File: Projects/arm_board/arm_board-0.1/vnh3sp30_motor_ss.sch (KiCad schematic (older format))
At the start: 3 parts

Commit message: Arm Board: bug fixes, and added footprints
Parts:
- removed P?: CONN_6, ~, symbol CONN_6
- added P1: CONN_5, ArmFootprints:5-pin_640467-1, symbol CONN_5
- added R23: 4.7k, Resistors_SMD:R_0805, symbol R
- added R39, R40: 1k, Resistors_SMD:R_0805, symbol R
- U14: renamed from U?; footprint (none) -> ArmFootprints:SN74LVC2G08DCTR
- VNH3: renamed from VNH1; footprint (none) -> ArmFootprints:VNH3SP30TR-E
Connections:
- net labels added: NOISE_5V, n_CNT_RESET
- net labels removed: CNT_RESET, EN
- wire segments 66 -> 71
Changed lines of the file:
@@
 LIBS:ArmComponentLibrary
 LIBS:arm_board-cache
-EELAYER 27 0
+EELAYER 25 0
 EELAYER END
 $Descr A4 11693 8268
@@
 $EndDescr
 $Comp
-L VNH3SP30 VNH1
+L VNH3SP30 VNH3
 U 1 1 564A6239
 P 8550 3800
-AR Path="/564B31DF/564A6239" Ref="VNH1"  Part="1"
-AR Path="/56666F75/564A6239" Ref="VNH1"  Part="1"
-AR Path="/56669634/564A6239" Ref="VNH1"  Part="1"
-AR Path="/56669644/564A6239" Ref="VNH1"  Part="1"
-AR Path="/5666D2E0/564A6239" Ref="VNH1"  Part="1"
-AR Path="/5666D2F0/564A6239" Ref="VNH1"  Part="1"
-AR Path="/56F5245F/564A6239" Ref="VNH1"  Part="1"
-AR Path="/56F544AF/564A6239" Ref="VNH1"  Part="1"
-F 0 "VNH1" H 9250 2850 60  0000 C CNN
+AR Path="/56F5245F/564A6239" Ref="VNH3"  Part="1"
+AR Path="/56F53B7D/564A6239" Ref="VNH4"  Part="1"
+AR Path="/56F544AF/564A6239" Ref="VNH5"  Part="1"
+AR Path="/56F55E0D/564A6239" Ref="VNH6"  Part="1"
+AR Path="/56F56B2F/564A6239" Ref="VNH7"  Part="1"
+F 0 "VNH4" H 9250 2850 60  0000 C CNN
 F 1 "VNH3SP30" H 8550 3800 60  0000 C CNN
-F 2 "" H 6950 3600 60  0000 C CNN
+F 2 "ArmFootprints:VNH3SP30TR-E" H 6950 3600 60  0001 C CNN
 F 3 "" H 6950 3600 60  0000 C CNN
 	1    8550 3800
@@
 	8550 5250 8550 4900
 Connection ~ 8550 4900
-Text HLabel 7250 3750 0    60   Input ~ 0
+Text HLabel 6800 3750 0    60   Input ~ 0
 DIR
-Text HLabel 7250 3850 0    60   Input ~ 0
+Text HLabel 6650 3850 0    60   Input ~ 0
 n_DIR
 Text HLabel 7250 4000 0    60   Input ~ 0
@@
 Wire Wire Line
 	7250 4000 7700 4000
-Wire Wire Line
-	7250 3850 7700 3850
-Wire Wire Line
-	7250 3750 7700 3750
-Wire Wire Line
-	7250 3500 7700 3500
 $Sheet
 S 5250 4600 1100 1000
@@
 F5 "CNT_UP" I L 5250 4700 60
 F6 "CNT_DWN" I L 5250 4800 60
-F7 "RESET" I L 5250 5000 60
-F8 "S0" I L 5250 5200 60
-F9 "S1" I L 5250 5300 60
-F10 "S2" I L 5250 5400 60
-F11 "S3" I L 5250 5500 60
+F7 "S0" I L 5250 5200 60
+F8 "S1" I L 5250 5300 60
+F9 "S2" I L 5250 5400 60
+F10 "S3" I L 5250 5500 60
+F11 "n_RESET" I L 5250 5000 60
 $EndSheet
 Wire Wire Line
@@
 	7550 3600 7550 3500
 Connection ~ 7550 3500
-Text HLabel 7250 3500 0    60   Input ~ 0
-EN
-Text Label 7350 3750 0    60   ~ 0
+Text Label 6750 3600 2    60   ~ 0
 DIR
-Text Label 7350 3850 0    60   ~ 0
+Text Label 6650 4050 2    60   ~ 0
 n_DIR
 $Comp
-L 74LVC2G08 U?
+L 74LVC2G08 U14
 U 1 1 565DD202
 P 4650 4850
-AR Path="/564B31DF/565DD202" Ref="U?"  Part="1"
-AR Path="/56666F75/565DD202" Ref="U?"  Part="1"
-AR Path="/56669634/565DD202" Ref="U?"  Part="1"
-AR Path="/56669644/565DD202" Ref="U?"  Part="1"
-AR Path="/5666D2E0/565DD202" Ref="U?"  Part="1"
-AR Path="/5666D2F0/565DD202" Ref="U?"  Part="1"
-AR Path="/56F5245F/565DD202" Ref="U?"  Part="1"
-AR Path="/56F544AF/565DD202" Ref="U?"  Part="1"
-F 0 "U?" H 4750 4450 60  0000 C CNN
+AR Path="/56F5245F/565DD202" Ref="U14"  Part="1"
+AR Path="/56F53B7D/565DD202" Ref="U21"  Part="1"
+AR Path="/56F544AF/565DD202" Ref="U28"  Part="1"
+AR Path="/56F55E0D/565DD202" Ref="U35"  Part="1"
+AR Path="/56F56B2F/565DD202" Ref="U42"  Part="1"
+F 0 "U21" H 4750 4450 60  0000 C CNN
 F 1 "74LVC2G08" V 4500 4900 60  0000 C CNN
-F 2 "" H 4650 4850 60  0000 C CNN
+F 2 "ArmFootprints:SN74LVC2G08DCTR" H 4650 4850 60  0001 C CNN
 F 3 "" H 4650 4850 60  0000 C CNN
 	1    4650 4850
@@
 CNT_UDRFLW
 Text HLabel 4850 5650 0    60   Output ~ 0
-CNT_RESET
+n_CNT_RESET
 Text HLabel 4850 5750 0    60   Output ~ 0
 CNT_S0
@@
 	9400 3950 9400 4150
 Connection ~ 9400 4050
-$Comp
-L CONN_6 P?
-U 1 1 56F466A7
-P 10750 5750
-AR Path="/564B31DF/56F466A7" Ref="P?"  Part="1"
-AR Path="/56F5245F/56F466A7" Ref="P?"  Part="1"
-AR Path="/56F544AF/56F466A7" Ref="P?"  Part="1"
-F 0 "P?" V 10700 5750 60  0000 C CNN
-F 1 "CONN_6" V 10800 5750 60  0000 C CNN
-F 2 "~" H 10750 5750 60  0000 C CNN
-F 3 "~" H 10750 5750 60  0000 C CNN
-	1    10750 5750
-	1    0    0    -1
-$EndComp
 Wire Wire Line
 	9800 3550 9800 5500
@@
 Wire Wire Line
 	9700 4050 9400 4050
+$Comp
+L R R39
+U 1 1 56C5F3D4
+P 7450 3750
+AR Path="/56F53B7D/56C5F3D4" Ref="R39"  Part="1"
+AR Path="/56F5245F/56C5F3D4" Ref="R24"  Part="1"
+AR Path="/56F544AF/56C5F3D4" Ref="R27"  Part="1"
+AR Path="/56F55E0D/56C5F3D4" Ref="R30"  Part="1"
+AR Path="/56F56B2F/56C5F3D4" Ref="R33"  Part="1"
+F 0 "R39" V 7530 3750 40  0000 C CNN
+F 1 "1k" V 7457 3751 40  0000 C CNN
+F 2 "Resistors_SMD:R_0805" V 7380 3750 30  0001 C CNN
+F 3 "" H 7450 3750 30  0000 C CNN
+	1    7450 3750
+	0    1    1    0
+$EndComp
+Wire Wire Line
+	6800 3750 7200 3750
+Wire Wire Line
+	6750 3600 6900 3600
+Wire Wire Line
+	6900 3600 6900 3750
+Connection ~ 6900 3750
+$Comp
+L R R40
+U 1 1 56C5F9C5
+P 7450 3850
+AR Path="/56F53B7D/56C5F9C5" Ref="R40"  Part="1"
+AR Path="/56F5245F/56C5F9C5" Ref="R25"  Part="1"
+AR Path="/56F544AF/56C5F9C5" Ref="R28"  Part="1"
+AR Path="/56F55E0D/56C5F9C5" Ref="R31"  Part="1"
+AR Path="/56F56B2F/56C5F9C5" Ref="R34"  Part="1"
+F 0 "R40" V 7530 3850 40  0000 C CNN
+F 1 "1k" V 7457 3851 40  0000 C CNN
+F 2 "Resistors_SMD:R_0805" V 7380 3850 30  0001 C CNN
+F 3 "" H 7450 3850 30  0000 C CNN
+	1    7450 3850
+	0    1    1    0
+$EndComp
+Wire Wire Line
+	7200 3850 6650 3850
+Wire Wire Line
+	6650 4050 6800 4050
+Wire Wire Line
+	6800 4050 6800 3850
+Connection ~ 6800 3850
+Wire Wire Line
+	7550 3500 7700 3500
+$Comp
+L R R23
+U 1 1 56C6696F
+P 7300 3500
+AR Path="/56F5245F/56C6696F" Ref="R23"  Part="1"
+AR Path="/56F544AF/56C6696F" Ref="R26"  Part="1"
+AR Path="/56F55E0D/56C6696F" Ref="R29"  Part="1"
+AR Path="/56F56B2F/56C6696F" Ref="R32"  Part="1"
+AR Path="/56F53B7D/56C6696F" Ref="R38"  Part="1"
+F 0 "R38" V 7380 3500 40  0000 C CNN
+F 1 "4.7k" V 7307 3501 40  0000 C CNN
+F 2 "Resistors_SMD:R_0805" V 7230 3500 30  0001 C CNN
+F 3 "" H 7300 3500 30  0000 C CNN
+	1    7300 3500
+	0    1    1    0
+$EndComp
+Text GLabel 7050 3250 1    60   Input ~ 0
+NOISE_5V
+Wire Wire Line
+	7050 3250 7050 3500
+$Comp
+L CONN_5 P1
+U 1 1 56CA7E11
+P 10800 5700
+AR Path="/56F5245F/56CA7E11" Ref="P1"  Part="1"
+AR Path="/56F53B7D/56CA7E11" Ref="P10"  Part="1"
+AR Path="/56F544AF/56CA7E11" Ref="P2"  Part="1"
+AR Path="/56F55E0D/56CA7E11" Ref="P7"  Part="1"
+AR Path="/56F56B2F/56CA7E11" Ref="P8"  Part="1"
+F 0 "P10" V 10750 5700 50  0000 C CNN
+F 1 "CONN_5" V 10850 5700 50  0000 C CNN
+F 2 "ArmFootprints:5-pin_640467-1" H 10800 5700 60  0001 C CNN
+F 3 "" H 10800 5700 60  0000 C CNN
+	1    10800 5700
+	1    0    0    -1
+$EndComp
 $EndSCHEMATC

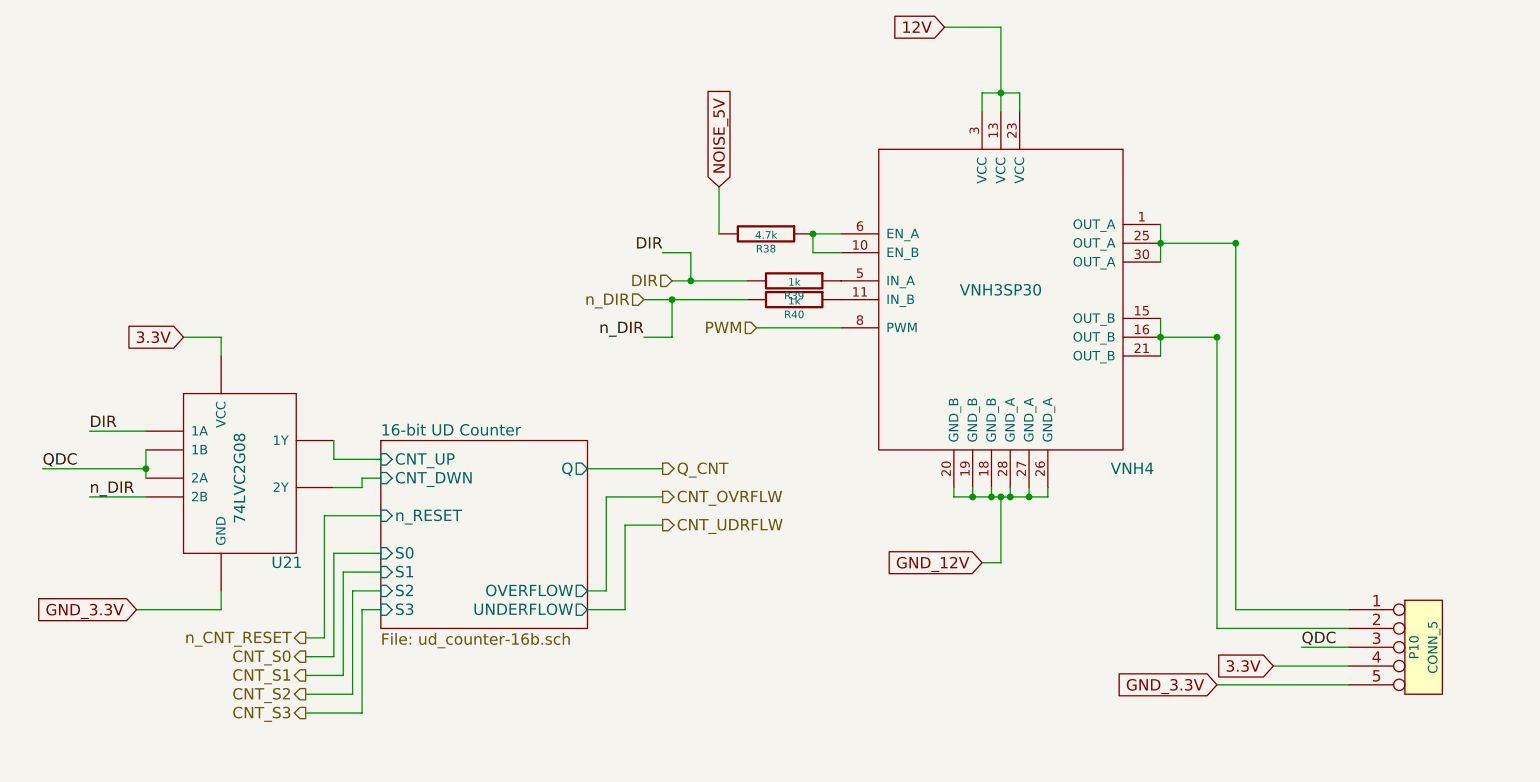
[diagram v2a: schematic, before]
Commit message: Arm Board: bug fixes, cleanup, and start PCB layout
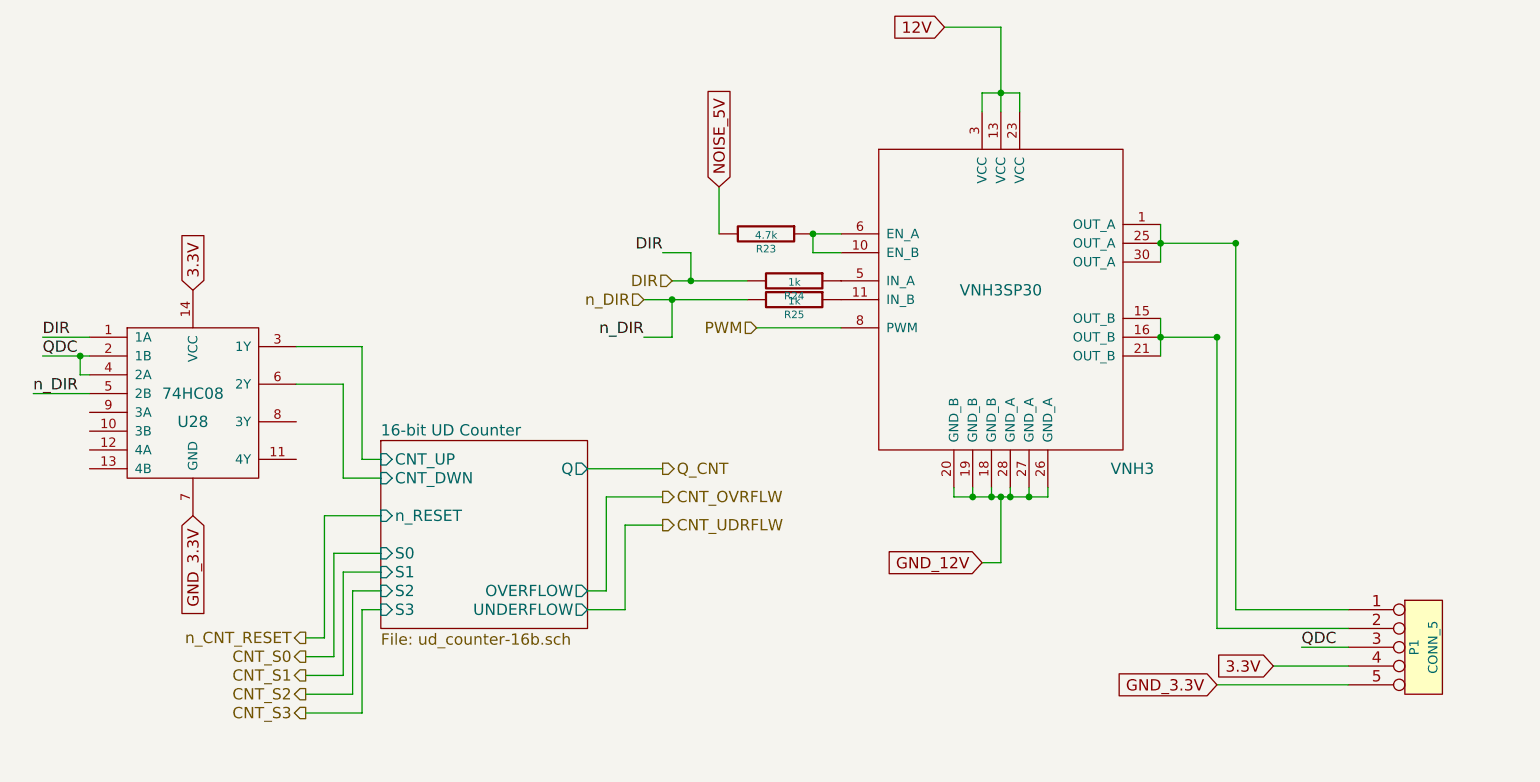
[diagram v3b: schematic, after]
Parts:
- removed U14: 74LVC2G08, ArmFootprints:SN74LVC2G08DCTR, symbol 74LVC2G08
- added U28: 74HC08, SMD_Packages:SOIC-14_N, symbol 74HC08
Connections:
- net 16-bit UD Counter/CNT_DWN: now also U28.6 (2Y)
- net 16-bit UD Counter/CNT_UP: now also U28.3 (1Y)
- net 3.3V: now also U28.14 (VCC)
- net DIR: now also U28.1 (1A)
- net GND_3.3V: now also U28.7 (GND)
- net QDC: now also U28.2 (1B), U28.4 (2A)
- net n_DIR: now also U28.5 (2B)
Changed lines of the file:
@@
 AR Path="/56F55E0D/564A6239" Ref="VNH6"  Part="1"
 AR Path="/56F56B2F/564A6239" Ref="VNH7"  Part="1"
-F 0 "VNH4" H 9250 2850 60  0000 C CNN
+F 0 "VNH3" H 9250 2850 60  0000 C CNN
 F 1 "VNH3SP30" H 8550 3800 60  0000 C CNN
 F 2 "ArmFootprints:VNH3SP30TR-E" H 6950 3600 60  0001 C CNN
@@
 Text Label 6650 4050 2    60   ~ 0
 n_DIR
-$Comp
-L 74LVC2G08 U14
-U 1 1 565DD202
-P 4650 4850
-AR Path="/56F5245F/565DD202" Ref="U14"  Part="1"
-AR Path="/56F53B7D/565DD202" Ref="U21"  Part="1"
-AR Path="/56F544AF/565DD202" Ref="U28"  Part="1"
-AR Path="/56F55E0D/565DD202" Ref="U35"  Part="1"
-AR Path="/56F56B2F/565DD202" Ref="U42"  Part="1"
-F 0 "U21" H 4750 4450 60  0000 C CNN
-F 1 "74LVC2G08" V 4500 4900 60  0000 C CNN
-F 2 "ArmFootprints:SN74LVC2G08DCTR" H 4650 4850 60  0001 C CNN
-F 3 "" H 4650 4850 60  0000 C CNN
-	1    4650 4850
-	1    0    0    -1
-$EndComp
-Text Label 3450 4750 0    60   ~ 0
-QDC
-Wire Wire Line
-	3450 4750 4000 4750
-Wire Wire Line
-	4000 4650 4000 4800
-Connection ~ 4000 4750
-Text Label 3700 4550 0    60   ~ 0
-DIR
-Text Label 3700 4900 0    60   ~ 0
-n_DIR
-Wire Wire Line
-	3700 4900 4000 4900
-Wire Wire Line
-	4000 4550 3700 4550
-Text GLabel 4200 4050 0    60   Input ~ 0
-3.3V
-Wire Wire Line
-	4200 4050 4400 4050
-Wire Wire Line
-	4400 4050 4400 4150
-Text GLabel 3950 5500 0    60   Input ~ 0
-GND_3.3V
-Wire Wire Line
-	3950 5500 4400 5500
-Wire Wire Line
-	4400 5500 4400 5400
-Wire Wire Line
-	5000 4600 5000 4700
-Wire Wire Line
-	5000 4700 5250 4700
-Wire Wire Line
-	5000 4850 5150 4850
-Wire Wire Line
-	5150 4850 5150 4800
-Wire Wire Line
-	5150 4800 5250 4800
 Text HLabel 6750 4750 2    60   Output ~ 0
 Q_CNT
@@
 AR Path="/56F55E0D/56C5F3D4" Ref="R30"  Part="1"
 AR Path="/56F56B2F/56C5F3D4" Ref="R33"  Part="1"
-F 0 "R39" V 7530 3750 40  0000 C CNN
+F 0 "R24" V 7530 3750 40  0000 C CNN
 F 1 "1k" V 7457 3751 40  0000 C CNN
 F 2 "Resistors_SMD:R_0805" V 7380 3750 30  0001 C CNN
@@
 AR Path="/56F55E0D/56C5F9C5" Ref="R31"  Part="1"
 AR Path="/56F56B2F/56C5F9C5" Ref="R34"  Part="1"
-F 0 "R40" V 7530 3850 40  0000 C CNN
+F 0 "R25" V 7530 3850 40  0000 C CNN
 F 1 "1k" V 7457 3851 40  0000 C CNN
 F 2 "Resistors_SMD:R_0805" V 7380 3850 30  0001 C CNN
@@
 AR Path="/56F56B2F/56C6696F" Ref="R32"  Part="1"
 AR Path="/56F53B7D/56C6696F" Ref="R38"  Part="1"
-F 0 "R38" V 7380 3500 40  0000 C CNN
+F 0 "R23" V 7380 3500 40  0000 C CNN
 F 1 "4.7k" V 7307 3501 40  0000 C CNN
 F 2 "Resistors_SMD:R_0805" V 7230 3500 30  0001 C CNN
@@
 AR Path="/56F55E0D/56CA7E11" Ref="P7"  Part="1"
 AR Path="/56F56B2F/56CA7E11" Ref="P8"  Part="1"
-F 0 "P10" V 10750 5700 50  0000 C CNN
+F 0 "P1" V 10750 5700 50  0000 C CNN
 F 1 "CONN_5" V 10850 5700 50  0000 C CNN
 F 2 "ArmFootprints:5-pin_640467-1" H 10800 5700 60  0001 C CNN
@@
 	1    0    0    -1
 $EndComp
+Text GLabel 4250 3800 1    60   Input ~ 0
+3.3V
+Text GLabel 4250 5000 3    60   Input ~ 0
+GND_3.3V
+$Comp
+L 74HC08 U28
+U 1 1 56CE991E
+P 4250 4350
+AR Path="/56F5245F/56CE991E" Ref="U28"  Part="1"
+AR Path="/56F53B7D/56CE991E" Ref="U58"  Part="1"
+AR Path="/56F544AF/56CE991E" Ref="U35"  Part="1"
+AR Path="/56F55E0D/56CE991E" Ref="U42"  Part="1"
+AR Path="/56F56B2F/56CE991E" Ref="U44"  Part="1"
+F 0 "U28" H 4250 4200 60  0000 C CNN
+F 1 "74HC08" H 4250 4350 60  0000 C CNN
+F 2 "SMD_Packages:SOIC-14_N" H 4250 4350 60  0001 C CNN
+F 3 "" H 4250 4350 60  0000 C CNN
+	1    4250 4350
+	1    0    0    -1
+$EndComp
+Text Label 3450 4150 0    60   ~ 0
+QDC
+Text Label 3450 4050 0    60   ~ 0
+DIR
+Text Label 3400 4350 0    60   ~ 0
+n_DIR
+Wire Wire Line
+	3450 4050 3700 4050
+Wire Wire Line
+	3450 4150 3700 4150
+Wire Wire Line
+	3650 4150 3650 4250
+Wire Wire Line
+	3650 4250 3700 4250
+Connection ~ 3650 4150
+Wire Wire Line
+	3400 4350 3700 4350
+Wire Wire Line
+	4800 4100 5150 4100
+Wire Wire Line
+	5150 4100 5150 4700
+Wire Wire Line
+	5150 4700 5250 4700
+Wire Wire Line
+	4800 4300 5050 4300
+Wire Wire Line
+	5050 4300 5050 4800
+Wire Wire Line
+	5050 4800 5250 4800
 $EndSCHEMATC

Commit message: Arm Board: finalizing footprints.
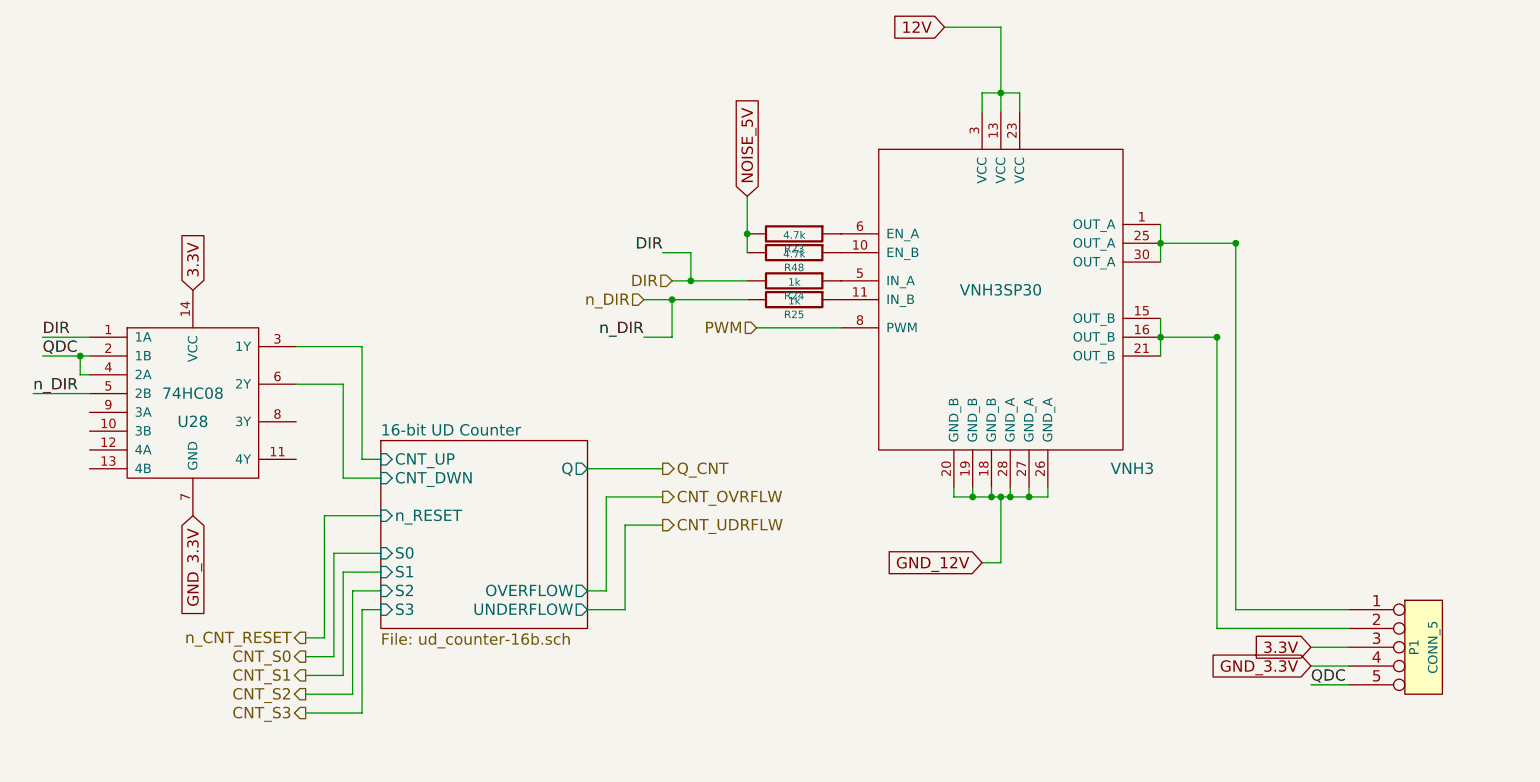
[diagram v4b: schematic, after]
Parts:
- added R53: 4.7k, Resistors_SMD:R_0805, symbol R
- U28: footprint SMD_Packages:SOIC-14_N -> ArmFootprints:SOIC-14
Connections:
- net 3.3V: now also P1.3; no longer P1.4
- net GND_3.3V: now also P1.4; no longer P1.5
- net NOISE_5V: now also R53.2
- net QDC: now also P1.5; no longer P1.3
- net at R23.1, VNH3.6 (EN_A): no longer VNH3.10 (EN_B)
- new net: R53.1, VNH3.10 (EN_B)
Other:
- moved on the sheet: R23
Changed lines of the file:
@@
 $Descr A4 11693 8268
 encoding utf-8
-Sheet 6 23
+Sheet 21 23
 Title ""
 Date "30 jan 2016"
@@
 F11 "n_RESET" I L 5250 5000 60
 $EndSheet
-Wire Wire Line
-	7700 3600 7550 3600
-Wire Wire Line
-	7550 3600 7550 3500
-Connection ~ 7550 3500
 Text Label 6750 3600 2    60   ~ 0
 DIR
@@
 	9700 5600 10400 5600
 Connection ~ 9700 4050
-Text Label 10150 5700 0    60   ~ 0
+Text Label 10200 5900 0    60   ~ 0
 QDC
-Wire Wire Line
-	10150 5700 10400 5700
-Text GLabel 10000 5800 0    60   Input ~ 0
+Text GLabel 10200 5700 0    60   Input ~ 0
 3.3V
-Wire Wire Line
-	10000 5800 10400 5800
-Text GLabel 9700 5900 0    60   Input ~ 0
+Text GLabel 10200 5800 0    60   Input ~ 0
 GND_3.3V
-Wire Wire Line
-	9700 5900 10400 5900
 Wire Wire Line
 	9400 3550 9800 3550
@@
 	6800 4050 6800 3850
 Connection ~ 6800 3850
-Wire Wire Line
-	7550 3500 7700 3500
 $Comp
 L R R23
 U 1 1 56C6696F
-P 7300 3500
+P 7450 3500
 AR Path="/56F5245F/56C6696F" Ref="R23"  Part="1"
 AR Path="/56F544AF/56C6696F" Ref="R26"  Part="1"
@@
 AR Path="/56F56B2F/56C6696F" Ref="R32"  Part="1"
 AR Path="/56F53B7D/56C6696F" Ref="R38"  Part="1"
-F 0 "R23" V 7380 3500 40  0000 C CNN
-F 1 "4.7k" V 7307 3501 40  0000 C CNN
-F 2 "Resistors_SMD:R_0805" V 7230 3500 30  0001 C CNN
-F 3 "" H 7300 3500 30  0000 C CNN
-	1    7300 3500
+F 0 "R23" V 7530 3500 40  0000 C CNN
+F 1 "4.7k" V 7457 3501 40  0000 C CNN
+F 2 "Resistors_SMD:R_0805" V 7380 3500 30  0001 C CNN
+F 3 "" H 7450 3500 30  0000 C CNN
+	1    7450 3500
 	0    1    1    0
 $EndComp
-Text GLabel 7050 3250 1    60   Input ~ 0
+Text GLabel 7200 3300 1    60   Input ~ 0
 NOISE_5V
-Wire Wire Line
-	7050 3250 7050 3500
 $Comp
 L CONN_5 P1
@@
 F 0 "U28" H 4250 4200 60  0000 C CNN
 F 1 "74HC08" H 4250 4350 60  0000 C CNN
-F 2 "SMD_Packages:SOIC-14_N" H 4250 4350 60  0001 C CNN
+F 2 "ArmFootprints:SOIC-14" H 4250 4350 60  0001 C CNN
 F 3 "" H 4250 4350 60  0000 C CNN
 	1    4250 4350
@@
 Wire Wire Line
 	5050 4800 5250 4800
+$Comp
+L R R53
+U 1 1 56E620A0
+P 7450 3600
+AR Path="/56F53B7D/56E620A0" Ref="R53"  Part="1"
+AR Path="/56F5245F/56E620A0" Ref="R48"  Part="1"
+AR Path="/56F544AF/56E620A0" Ref="R49"  Part="1"
+AR Path="/56F55E0D/56E620A0" Ref="R50"  Part="1"
+AR Path="/56F56B2F/56E620A0" Ref="R51"  Part="1"
+F 0 "R48" V 7530 3600 40  0000 C CNN
+F 1 "4.7k" V 7457 3601 40  0000 C CNN
+F 2 "Resistors_SMD:R_0805" V 7380 3600 30  0001 C CNN
+F 3 "" H 7450 3600 30  0000 C CNN
+	1    7450 3600
+	0    1    1    0
+$EndComp
+Wire Wire Line
+	7200 3300 7200 3600
+Connection ~ 7200 3500
+Wire Wire Line
+	10200 5800 10400 5800
+Wire Wire Line
+	10400 5700 10200 5700
+Wire Wire Line
+	10200 5900 10400 5900
 $EndSCHEMATC
